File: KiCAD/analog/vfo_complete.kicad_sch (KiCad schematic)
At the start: 19 parts, among them J1 Conn_Coaxial_Small, Q2 40673, U1 LM7171xIN, U5 Si5351A_Breakout

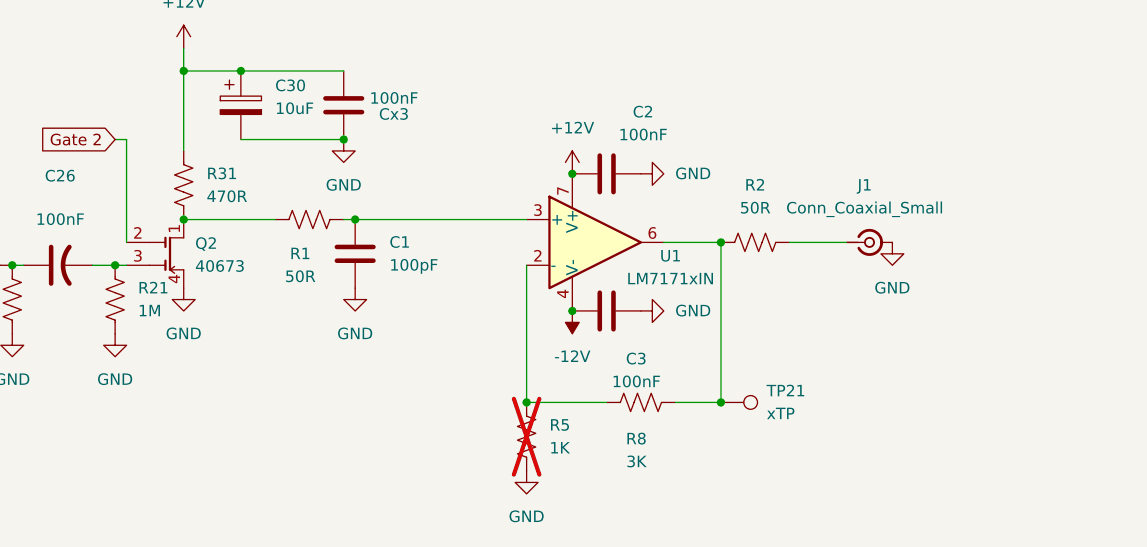
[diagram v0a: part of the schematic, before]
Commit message: revD: address PDF design-review items M2-M4 + archive review handoff
- Fix schematic issues M2-M4 flagged in the pre-layout design review:
  changes in KiCAD/analog/vfo_complete.kicad_sch and
  KiCAD/ss_pa/fault_shutdown.kicad_sch. M1 is a documentation-only
  item and does not require a schematic edit.
- Regenerate netlists for analog, ss_pa, Output LPF, frontpanel,
  protoshield.
- Add Documentation/revD_prelayout_review_handoff.md -- the handoff
  package used to brief the external reviewer (board-by-board summary,
  cross-board interconnects, specific review asks).
- Add Documentation/xmitter Rev D Pre-Layout Design Review-1.pdf --
  the reviewer's returned analysis, kept for traceability of future
  changes against the Must-Fix / Should-Consider / Nice-to-Have items.

Co-Authored-By: Claude Opus 4.7 <noreply@anthropic.com>
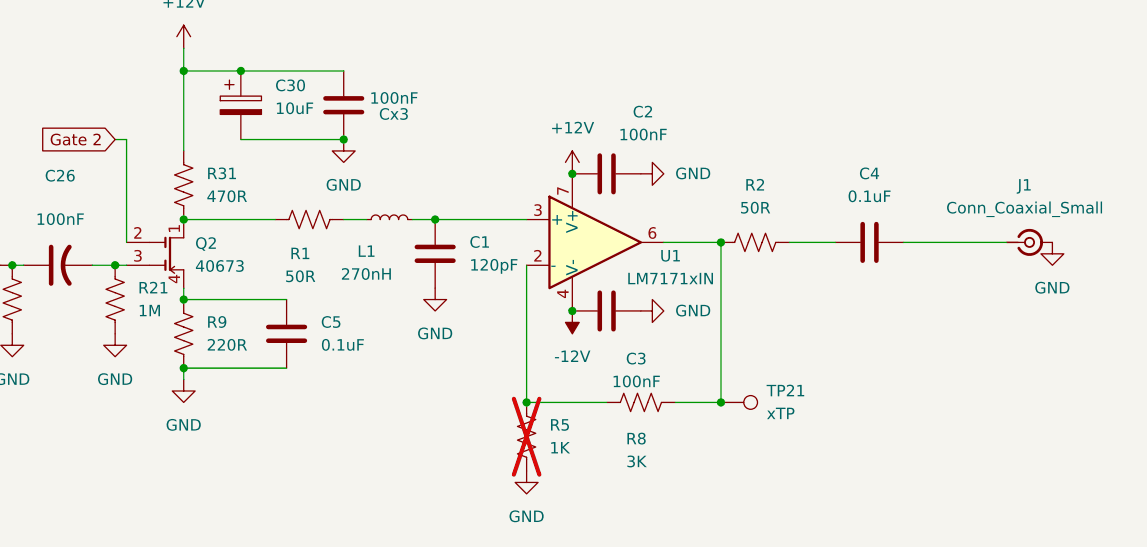
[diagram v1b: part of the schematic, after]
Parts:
- added C4, C5: 0.1uF, symbol Device:C
- added L1: 270nH, symbol Device:L_Small
- added R9: 220R, symbol Device:R_US
- C1: value 100pF -> 120pF
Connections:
- net GND: now also C5.2, R9.2; no longer Q2.4 (S)
- net at C1.1, U1.3 (+): now also L1.2; no longer R1.2
- net at R2.2: now also C4.1; no longer J1.1 (In)
- new net: L1.1, R1.2
- new net: C4.2, J1.1 (In)
- new net: C5.1, Q2.4 (S), R9.1
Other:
- moved on the sheet: C1, J1

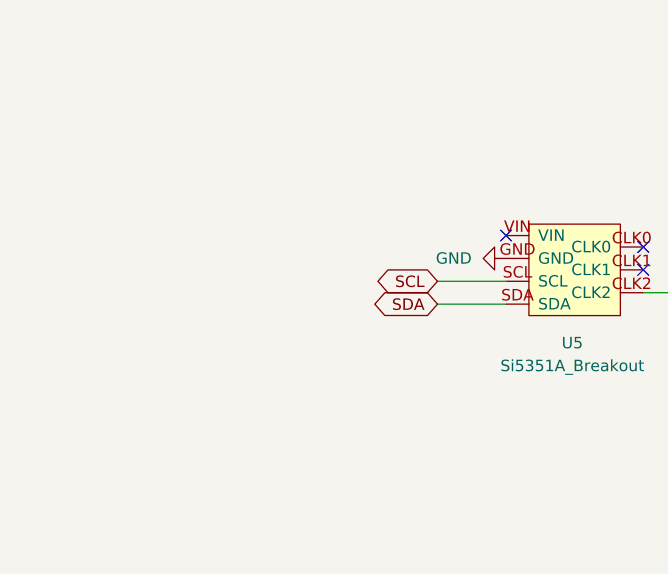
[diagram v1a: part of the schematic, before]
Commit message: revD analog: I2C level shifter for M6 + xmitter library additions
- Add Adafruit #757 BSS138 4-channel bidirectional I2C level shifter
  at the Si5351 I2C entry point on analog. Metro drives LV1/LV2 at
  +3.3V, the shared I2C bus (U17 PCF8575 analog, PCF8575 + MCP4725
  frontpanel, Si5351, MCP4728) runs at +5V on the HV side.
- Local 0.1 uF decoupling at LV and HV pins of the breakout.
- xmitter library additions:
    * symbol:    Adafruit_757_LevelShifter (12-pin breakout, LV side
                 pins 1-6, HV side pins 7-12, pre-linked to footprint)
    * footprint: Adafruit_757_BSS138_LevelShifter (2x6 header pattern,
                 2.54 mm pitch, 12.7 mm row-to-row, 1.0 mm NPTH holes.
                 Row spacing VERIFY against physical stock before fab.)
- M7 fix: MCP4922 (U4) VDD moved to +3.3V so Metro's 3.3V SPI meets
  the DAC's logic-high threshold (V_IH = 0.7*VDD = 2.31V @ 3.3V, well
  below Metro's 3.3V output). V_REF <= 3.3V still ample for G2
  envelope and BS170 bias.

Co-Authored-By: Claude Opus 4.7 <noreply@anthropic.com>
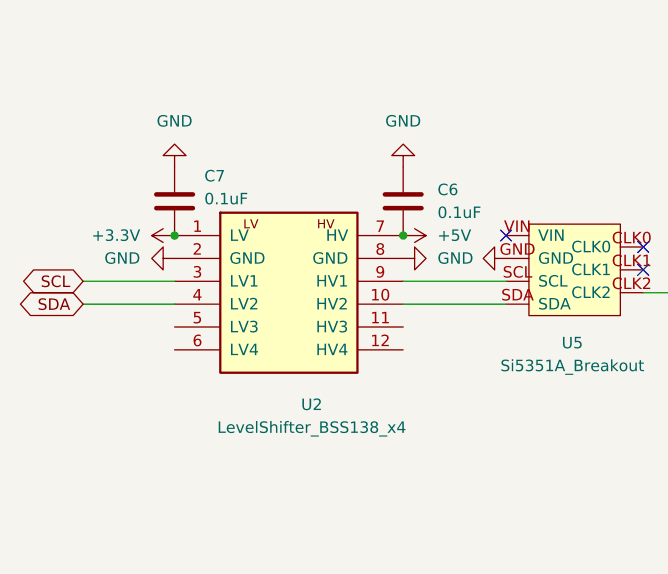
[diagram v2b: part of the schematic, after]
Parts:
- added C6, C7: 0.1uF, symbol Device:C
- added U2: LevelShifter_BSS138_x4, xmitter:Adafruit_757_BSS138_LevelShifter, symbol xmitter:Adafruit_757_LevelShifter
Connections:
- net GND: now also C6.1, C7.1, U2.2 (GND), U2.8 (GND)
- net SCL: now also U2.3 (LV1); no longer U5.SCL
- net SDA: now also U2.4 (LV2); no longer U5.SDA
- new net: U2.10 (HV2), U5.SDA
- new net: U2.9 (HV1), U5.SCL
- new net +3.3V: C7.2, U2.1 (LV)
- new net +5V: C6.2, U2.7 (HV)

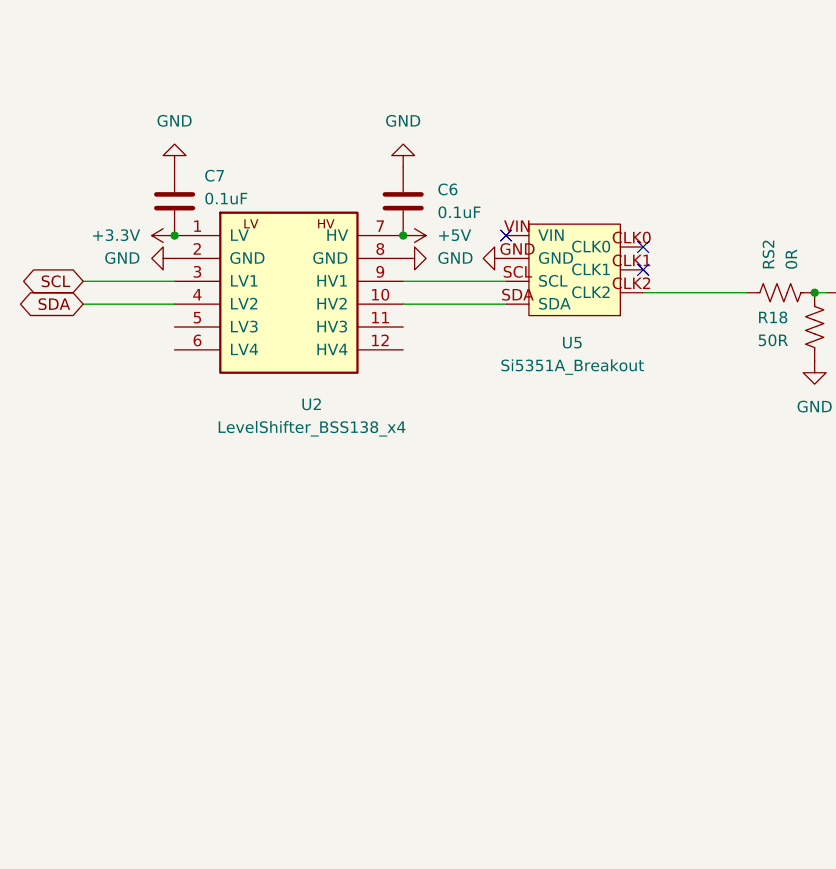
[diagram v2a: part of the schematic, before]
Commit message: revD: ss_pa Option C 5V rail + analog SW1 THT + R/C footprints + doc refresh
ss_pa Option C: swap U13 to LM2936Z-5.0 (full +5V logic rail), re-size
R10 10K->6.8K to preserve ~0.3V fault trip at new rail, drop +3.3V net
entirely. Fixes the previously-dead +5V bus that had no source.

Analog SW1 (Si5351 bringup DPDT): swap SMD footprint for
Button_Switch_THT:SW_CK_JS202011CQN_DPDT_Straight. Verified pin-numbering
convention (pin 1 above pin 6 in THT) matches user's intended DPST
wiring; both SDA/SCL break together.

Analog: assign missing footprints to R3/R4/R5/R8/R9 (DIN0207 axial) and
C4/C5/C6/C7/C8 (disc ceramic 5mm). Add xmitter:DIP-14_W7.62mm.kicad_mod
and 74HCT125 symbol to the xmitter library.

Documentation: Rev D handoff doc updated with M1-M8 fix status, Option C
notes, I2C bus voltage architecture, 74HCT125 SPI shifter, FAULT_N
divider details, and Metro-no-footprint note. Supporting docs updated:
i2c_bus.md full rewrite for 5V HV bus + STEMMA reroute, revD_interconnect
board inventory refresh, status banners on ss_pa.md / Master_Description /
cw_envelope_keyer / front_panel_interface pointing to handoff doc for
items beyond their last-current date.

Co-Authored-By: Claude Opus 4.7 <noreply@anthropic.com>
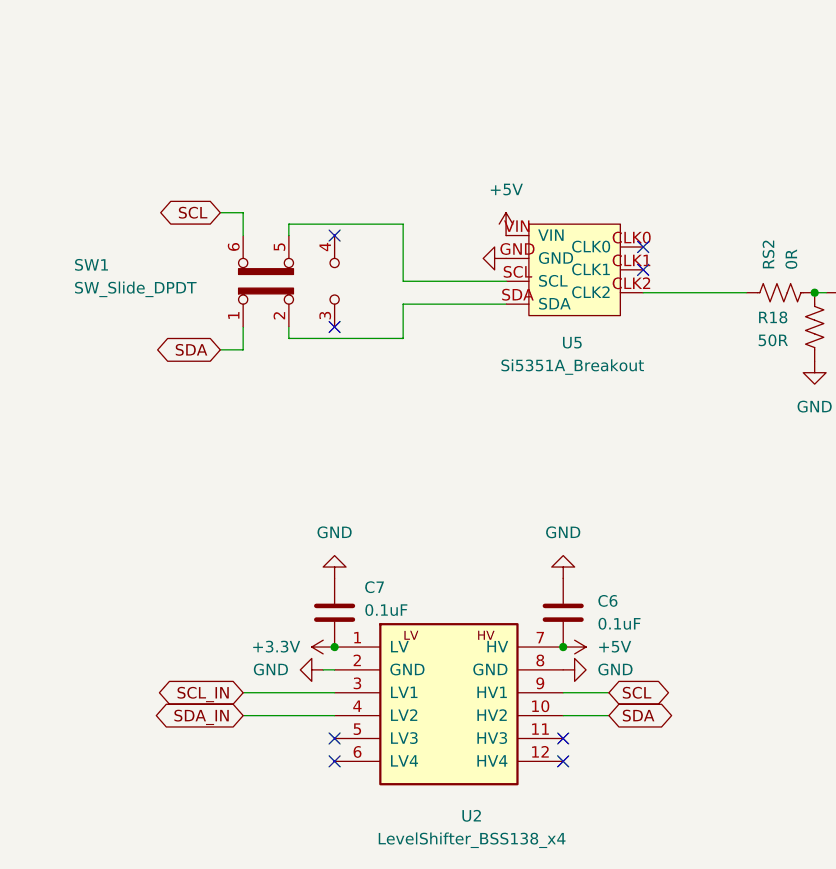
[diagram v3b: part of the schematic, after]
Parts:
- added SW1: SW_Slide_DPDT, Button_Switch_THT:SW_CK_JS202011CQN_DPDT_Straight, symbol Switch:SW_Slide_DPDT
- C4, C5, C6, C7: footprint (none) -> Capacitor_THT:C_Disc_D5.0mm_W2.5mm_P5.00mm
- R5, R8, R9: footprint (none) -> Resistor_THT:R_Axial_DIN0207_L6.3mm_D2.5mm_P10.16mm_Horizontal
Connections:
- net +5V: now also U5.VIN
- net SCL: now also U2.9 (HV1), SW1.6 (C); no longer U2.3 (LV1)
- net SDA: now also U2.10 (HV2), SW1.1 (A); no longer U2.4 (LV2)
- net at U5.SDA: now also SW1.2 (B); no longer U2.10 (HV2)
- net at U5.SCL: now also SW1.5 (B); no longer U2.9 (HV1)
- new net SCL_IN: U2.3 (LV1)
- new net SDA_IN: U2.4 (LV2)
- no-connect marks 3 -> 8

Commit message: revD analog: A1 Done - vfo_complete small adds (C9, R11, #PWR56)
Marks analog phase A1 complete.

Co-Authored-By: Claude Opus 4.7 <noreply@anthropic.com>
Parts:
- added C9: 10nF, symbol Device:C
- added R11: 10K, symbol Device:R_US
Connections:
- net GND: now also R11.1
- net at C1.1, L1.2, U1.3 (+): now also R11.2
- net at Q2.1 (D), R31.2: now also C9.1; no longer R1.1
- new net: C9.2, R1.1
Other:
- moved on the sheet: R1

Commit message: revD analog: DGFET op-amp offset-mute topology + doc updates
Retire the Q11/Q12 PNP KeyUp mute path on the DGFET keyer G2 (sim showed
only ~2.6:1 on/off ratio with G1 biased above V_TO). Replace with an
LM7171 (U10) non-inverting op-amp wired as DC offset:
  V_G2 = V_DAC * (1 + R20/R23) - V_ref * (R20/R23)
with V_ref ~5.05V (1N4733A Zener D2, R24 1K bias, R25 1K / R32 100K
summing divider) and R20=6.2K / R23=10K (G=0.62). DAC=0 drives G2 to
-3.1V (fully cuts off the 40673, sim-verified 12pA leakage, ~10^9 on/off
ratio); DAC=5V drives G2 to +5V (matches prior keyed operating point).
KEY_UP net eliminated -- mute is intrinsic to the signal path, firmware
controls RF enable/disable solely via what it writes to the MCP4921
envelope channel.

Includes new test.kicad_sch sheet carrying the U10/R20-R32 subcircuit.

Doc updates: CLAUDE.md DGFET section rewritten; handoff doc gets a new
"DGFET keyer mute topology" section explaining retirement reason and
new transfer function; Master_Description Sec 2 and SPI-bus section
updated; revD_interconnect G2 amplitude-control block updated;
control_board_functional_blocks.md gets a prominent retirement banner
pointing at the current scheme.

Co-Authored-By: Claude Opus 4.7 <noreply@anthropic.com>
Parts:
- added C10: 100nF, symbol Device:C
- added R14, R19: R_US, symbol Device:R_US
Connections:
- net +12V: now also R14.1
- net GND: now also C10.2, R19.2; no longer R21.2
- new net: C10.1, R14.2, R19.1, R21.2
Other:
- moved on the sheet: R21

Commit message: revD: analog + ss_pa RF filtering on umbilical signals
ss_pa: 1 uH RFC + bypass cap(s) added on each umbilical-crossing signal
to attenuate 14 MHz ingress from the cable and keep hot IRF510-source
RF from being injected back into the umbilical:

- PA_Bias_A_Raw: L6 1uH + C13 100nF + C26 100pF at J31.7
- PA_Bias_B_Raw: L7 1uH + C22 100nF + C27 100pF at J31.8
- Source_Sense_A: L8 1uH + C23 100nF between IRF510A source tap and
  the shared comparator/ADC node (new Source_Sense_A_Raw holds the
  Kelvin sense resistors R1/R2)
- Source_Sense_B: L9 1uH + C24 100nF, mirror of A on Q4 side
- DRIVER_BIAS: R20 100R + C19 0.1uF + C20 100pF already placed
  previously
- FAULT_N: R23 100R + C25 100pF filter on the external side of the
  latch (LM393 outputs + R9 pullup remain on the internal node for
  fast latching, R23 isolates from umbilical and 4066 enables)

Attenuation ~40-60 dB at 14 MHz across all five umbilical signals.

Analog: companion schematic touches for the DGFET G2 op-amp mute
subcircuit on the test sheet.

Co-Authored-By: Claude Opus 4.7 <noreply@anthropic.com>
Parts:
- added C23: 2pF, symbol Device:C
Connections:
- net at R5.1, R8.1, U1.2 (-): now also C23.1
- net at R2.1, R8.2, TP21.1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: now also C23.2
- net Gate 2 renamed GATE_2
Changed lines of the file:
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@@
 	)
 	(junction
+		(at 181.61 105.41)
+		(diameter 0)
+		(color 0 0 0 0)
+	)
+	(junction
 		(at 152.4 76.2)
 		(diameter 0)
@@
 	)
 	(junction
+		(at 189.23 105.41)
+		(diameter 0)
+		(color 0 0 0 0)
+	)
+	(junction
 		(at 134.62 85.09)
 		(diameter 0)
@@
 	(wire
 		(pts
+			(xy 189.23 105.41) (xy 189.23 110.49)
+		)
+		(stroke
+			(width 0)
+			(type default)
+		)
+	)
+	(wire
+		(pts
 			(xy 127 102.87) (xy 127 120.65)
 		)
@@
 	(wire
 		(pts
+			(xy 181.61 105.41) (xy 181.61 110.49)
+		)
+		(stroke
+			(width 0)
+			(type default)
+		)
+	)
+	(wire
+		(pts
 			(xy 134.62 102.87) (xy 134.62 101.6)
 		)
@@
 		)
 	)
-	(global_label "Gate 2"
+	(global_label "GATE_2"
 		(shape input)
 		(at 127 76.2 180)
@@
 		)
 		(property "Intersheetrefs" "${INTERSHEET_REFS}"
-			(at 117.6044 76.2 0)
+			(at 117.3625 76.2 0)
 			(hide yes)
 			(show_name no)
@@
 		(dnp no)
 		(property "Reference" "C3"
-			(at 184.912 100.584 90)
+			(at 189.738 98.298 90)
 			(show_name no)
 			(do_not_autoplace no)
@@
 		)
 		(property "Value" "100nF"
-			(at 184.912 103.124 90)
+			(at 189.738 100.838 90)
 			(show_name no)
 			(do_not_autoplace no)
@@
 	)
 	(symbol
+		(lib_id "Device:C")
+		(at 185.42 110.49 90)
+		(unit 1)
+		(body_style 1)
+		(exclude_from_sim no)
+		(in_bom yes)
+		(on_board yes)
+		(in_pos_files yes)
+		(dnp no)
+		(property "Reference" "C23"
+			(at 185.674 115.824 90)
+			(show_name no)
+			(do_not_autoplace no)
+			(effects
+				(font
+					(size 1.27 1.27)
+				)
+			)
+		)
+		(property "Value" "2pF"
+			(at 185.674 118.364 90)
+			(show_name no)
+			(do_not_autoplace no)
+			(effects
+				(font
+					(size 1.27 1.27)
+				)
+			)
+		)
+		(property "Footprint" ""
+			(at 189.23 109.5248 0)
+			(hide yes)
+			(show_name no)
+			(do_not_autoplace no)
+			(effects
+				(font
+					(size 1.27 1.27)
+				)
+			)
+		)
+		(property "Datasheet" ""
+			(at 185.42 110.49 0)
+			(hide yes)
+			(show_name no)
+			(do_not_autoplace no)
+			(effects
+				(font
+					(size 1.27 1.27)
+				)
+			)
+		)
+		(property "Description" "Unpolarized capacitor"
+			(at 185.42 110.49 0)
+			(hide yes)
+			(show_name no)
+			(do_not_autoplace no)
+			(effects
+				(font
+					(size 1.27 1.27)
+				)
+			)
+		)
+		(pin "1"
+		)
+		(pin "2"
+		)
+		(instances
+			(project "analog"
+				(path "/d3de40b8-856b-4fbd-829c-f45ffcd55742/94bbc356-fa50-4d6f-b6f0-2ea7eca96dd3"
+					(reference "C23")
+					(unit 1)
+				)
+			)
+		)
+	)
+	(symbol
 		(lib_id "Device:R_US")
 		(at 149.86 85.09 90)
@@
 		(dnp no)
 		(property "Reference" "R8"
-			(at 184.912 109.474 90)
+			(at 182.88 99.568 90)
 			(show_name no)
 			(do_not_autoplace no)
@@
 		)
 		(property "Value" "3K"
-			(at 184.912 112.014 90)
+			(at 182.88 102.108 90)
 			(show_name no)
 			(do_not_autoplace no)

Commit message: revD analog: L1 Bourns 78F footprint + CD74HC4050E xmitter lib additions
Analog L1 (270nH Bourns 78F RF choke) gets footprint
Inductor_THT:L_Axial_L7.0mm_D3.3mm_P10.16mm_Horizontal_Fastron_MICC
(stock KiCad; 78F body 7.11x2.79mm fits within the MICC silk envelope).

Added to xmitter library:
- symbol CD74HC4050E (hex non-inverting buffer, DIP-16, standard 4050
  pinout, pre-linked to xmitter:DIP-16_W7.62mm footprint)
- footprint xmitter:DIP-16_W7.62mm (verbatim copy of stock
  Package_DIP:DIP-16_W7.62mm so the lib is self-contained)

Other sheet / project / netlist touches picked up from the recent
session work on analog test sheet and protoshield.

Co-Authored-By: Claude Opus 4.7 <noreply@anthropic.com>
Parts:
- L1: footprint (none) -> Inductor_THT:L_Axial_L7.0mm_D3.3mm_P10.16mm_Horizontal_Fastron_MICC
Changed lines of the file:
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@@
 			)
 		)
-		(property "Footprint" ""
+		(property "Footprint" "Inductor_THT:L_Axial_L7.0mm_D3.3mm_P10.16mm_Horizontal_Fastron_MICC"
 			(at 157.48 85.09 0)
 			(hide yes)

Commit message: revD: footprint pass across all boards + ss_pa fault-chain fix + LLM review brief
- New tools/assign_misc_footprints.py: lib_id-keyed footprint assigner
  (resistors, screw terminals, pin headers, LT1054); mirrors cap-script
  safe-write (UTF-8 no BOM, no CRLF translation).
- tools/assign_cap_footprints.py: added 0.47uF -> C_Rect_L7.0mm case.
- Ran both scripts across analog, ss_pa, Output LPF, frontpanel,
  protoshield, and shelved power board. ~100 fills; details in diffs.
- ss_pa: R1-R4 (0.22 ohm source sense) upgraded to 2W Yageo RSF200
  with DIN0516 L15.5mm/P20.32mm footprint; Value tagged "0.22R 2W".
  R15/R16 confirmed 1/4W (DIN0207) for BS170 source degeneration.
- analog/power: R44 15R 5W horizontal, P30.48mm footprint.
- ss_pa fault chain (from external LLM review): R21/R22 raised
  10K -> 100K to restore self-latching loop gain; new R26 = 100K
  across C12 so cap discharges between power cycles (reliable reset).
  R26 footprint pending.
- Documentation/revD_llm_review_brief.md: new, comprehensive system
  description for external LLM deep-dive (function, component values,
  power dissipation, design flaws). References all five board netlists.

Co-Authored-By: Claude Opus 4.7 <noreply@anthropic.com>
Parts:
- C10: footprint (none) -> Capacitor_THT:C_Disc_D5.0mm_W2.5mm_P5.00mm
- C23: footprint (none) -> xmitter:C_Axial_Kemet_Aximax_C41X_L4.5mm_D2.6mm_P7.62mm_Horizontal
- C9: footprint (none) -> Capacitor_THT:C_Disc_D6.0mm_W2.5mm_P5.00mm
- R11, R14, R19: footprint (none) -> Resistor_THT:R_Axial_DIN0207_L6.3mm_D2.5mm_P10.16mm_Horizontal
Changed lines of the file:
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@@
 			)
 		)
-		(property "Footprint" ""
+		(property "Footprint" "Capacitor_THT:C_Disc_D5.0mm_W2.5mm_P5.00mm"
 			(at 134.3152 128.27 0)
 			(hide yes)
@@
 			)
 		)
-		(property "Footprint" ""
+		(property "Footprint" "Resistor_THT:R_Axial_DIN0207_L6.3mm_D2.5mm_P10.16mm_Horizontal"
 			(at 163.576 81.534 90)
 			(hide yes)
@@
 			)
 		)
-		(property "Footprint" ""
+		(property "Footprint" "Resistor_THT:R_Axial_DIN0207_L6.3mm_D2.5mm_P10.16mm_Horizontal"
 			(at 139.446 117.094 90)
 			(hide yes)
@@
 			)
 		)
-		(property "Footprint" ""
+		(property "Footprint" "Resistor_THT:R_Axial_DIN0207_L6.3mm_D2.5mm_P10.16mm_Horizontal"
 			(at 139.446 124.714 90)
 			(hide yes)
@@
 			)
 		)
-		(property "Footprint" ""
+		(property "Footprint" "Capacitor_THT:C_Disc_D6.0mm_W2.5mm_P5.00mm"
 			(at 146.05 84.1248 0)
 			(hide yes)
@@
 			)
 		)
-		(property "Footprint" ""
+		(property "Footprint" "xmitter:C_Axial_Kemet_Aximax_C41X_L4.5mm_D2.6mm_P7.62mm_Horizontal"
 			(at 189.23 109.5248 0)
 			(hide yes)
